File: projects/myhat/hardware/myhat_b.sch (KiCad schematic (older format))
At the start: 4 parts

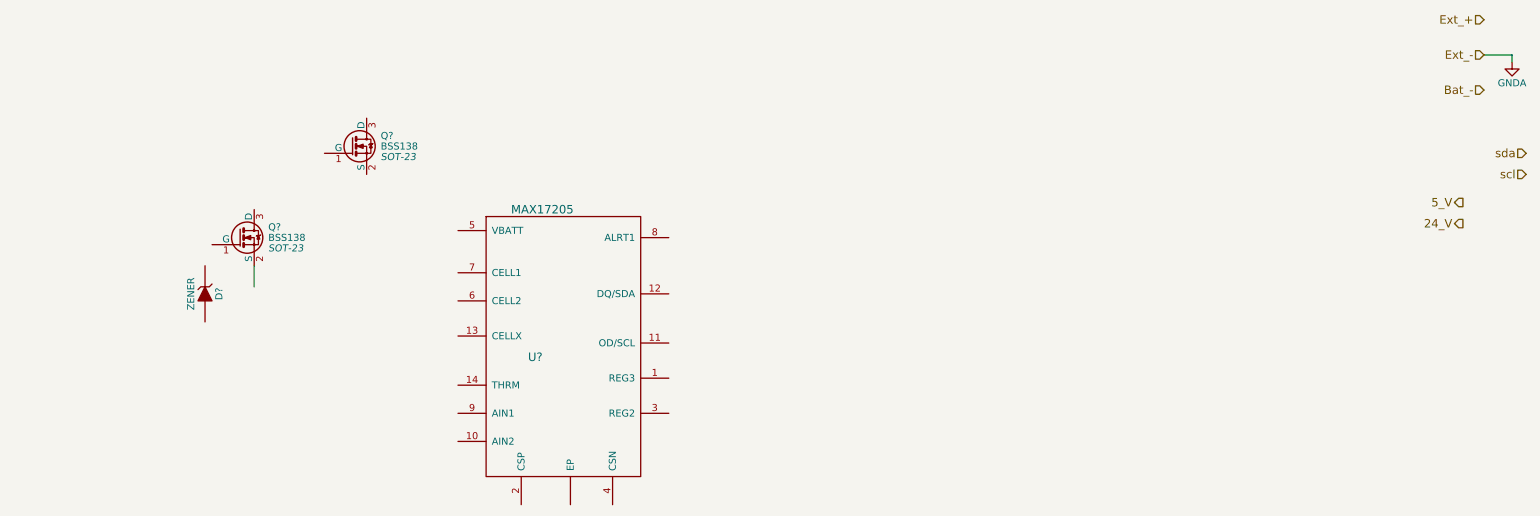
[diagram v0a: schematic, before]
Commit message: entered components on myhat for max17205
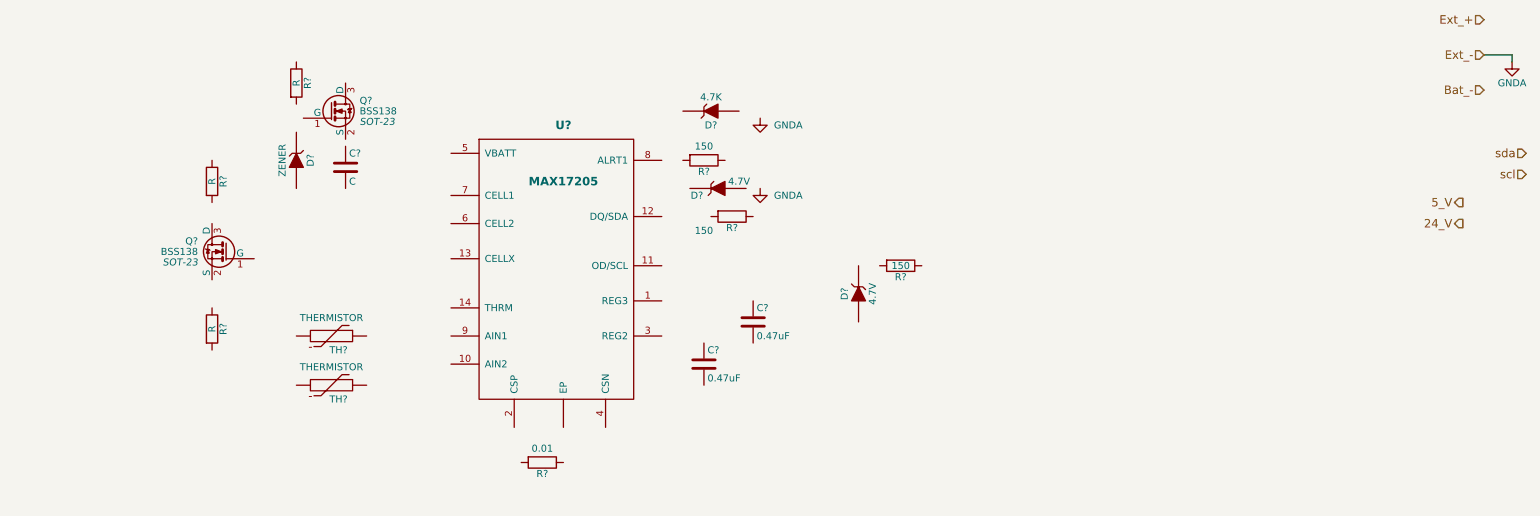
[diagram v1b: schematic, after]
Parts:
- removed U?: MAX17205, symbol MAX17205
- added C?: C, symbol C
- added C? (x2): 0.47uF, symbol C
- added D?: 4.7K, symbol ZENER
- added D? (x2): 4.7V, symbol ZENER
- added R? (x3): R, symbol R
- added R?: 0.01, symbol R
- added R? (x3): 150, symbol R
- added TH? (x2): THERMISTOR, symbol THERMISTOR
- added U?: MAX17205, symbol MAX17205
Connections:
- wire segments 3 -> 2
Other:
- moved on the sheet: D?, Q?
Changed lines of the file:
@@
 5_V
-$Comp
-L MAX17205 U?
-U 1 1 5838EF12
-P 3750 3550
-F 0 "U?" H 3400 3800 60  0000 C CNN
-F 1 "MAX17205" H 3450 4850 60  0000 C CNN
-F 2 "" H 3750 3550 60  0000 C CNN
-F 3 "" H 3750 3550 60  0000 C CNN
-	1    3750 3550
-	1    0    0    -1
-$EndComp
 $Comp
 L BSS138 Q?
 U 1 1 5838F608
-P 1300 2450
-F 0 "Q?" H 1500 2525 50  0000 L CNN
-F 1 "BSS138" H 1500 2450 50  0000 L CNN
-F 2 "SOT-23" H 1500 2375 50  0000 L CIN
-F 3 "" H 1300 2450 50  0000 L CNN
-	1    1300 2450
+P 1950 1550
+F 0 "Q?" H 2150 1625 50  0000 L CNN
+F 1 "BSS138" H 2150 1550 50  0000 L CNN
+F 2 "SOT-23" H 2150 1475 50  0000 L CIN
+F 3 "" H 1950 1550 50  0000 L CNN
+	1    1950 1550
 	1    0    0    -1
 $EndComp
@@
 L BSS138 Q?
 U 1 1 5838F9E4
-P 2100 1800
-F 0 "Q?" H 2300 1875 50  0000 L CNN
-F 1 "BSS138" H 2300 1800 50  0000 L CNN
-F 2 "SOT-23" H 2300 1725 50  0000 L CIN
-F 3 "" H 2100 1800 50  0000 L CNN
-	1    2100 1800
-	1    0    0    -1
-$EndComp
-Wire Wire Line
-	1400 2800 1400 2650
+P 1200 2550
+F 0 "Q?" H 1400 2625 50  0000 L CNN
+F 1 "BSS138" H 1400 2550 50  0000 L CNN
+F 2 "SOT-23" H 1400 2475 50  0000 L CIN
+F 3 "" H 1200 2550 50  0000 L CNN
+	1    1200 2550
+	-1   0    0    -1
+$EndComp
 $Comp
 L ZENER D?
 U 1 1 5839AB61
-P 1050 2850
-F 0 "D?" H 1050 2950 50  0000 C CNN
-F 1 "ZENER" H 1050 2750 50  0000 C CNN
-F 2 "" H 1050 2850 50  0000 C CNN
-F 3 "" H 1050 2850 50  0000 C CNN
-	1    1050 2850
+P 1700 1900
+F 0 "D?" H 1700 2000 50  0000 C CNN
+F 1 "ZENER" H 1700 1800 50  0000 C CNN
+F 2 "" H 1700 1900 50  0000 C CNN
+F 3 "" H 1700 1900 50  0000 C CNN
+	1    1700 1900
 	0    1    1    0
 $EndComp
@@
 Wire Wire Line
 	10350 1150 10350 1200
+$Comp
+L C C?
+U 1 1 583A4045
+P 2050 1950
+F 0 "C?" H 2075 2050 50  0000 L CNN
+F 1 "C" H 2075 1850 50  0000 L CNN
+F 2 "" H 2088 1800 50  0000 C CNN
+F 3 "" H 2050 1950 50  0000 C CNN
+	1    2050 1950
+	1    0    0    -1
+$EndComp
+$Comp
+L R R?
+U 1 1 583A42D9
+P 1100 2050
+F 0 "R?" V 1180 2050 50  0000 C CNN
+F 1 "R" V 1100 2050 50  0000 C CNN
+F 2 "" V 1030 2050 50  0000 C CNN
+F 3 "" H 1100 2050 50  0000 C CNN
+	1    1100 2050
+	1    0    0    -1
+$EndComp
+$Comp
+L R R?
+U 1 1 583A4306
+P 1700 1350
+F 0 "R?" V 1780 1350 50  0000 C CNN
+F 1 "R" V 1700 1350 50  0000 C CNN
+F 2 "" V 1630 1350 50  0000 C CNN
+F 3 "" H 1700 1350 50  0000 C CNN
+	1    1700 1350
+	1    0    0    -1
+$EndComp
+$Comp
+L R R?
+U 1 1 583A4395
+P 1100 3100
+F 0 "R?" V 1180 3100 50  0000 C CNN
+F 1 "R" V 1100 3100 50  0000 C CNN
+F 2 "" V 1030 3100 50  0000 C CNN
+F 3 "" H 1100 3100 50  0000 C CNN
+	1    1100 3100
+	1    0    0    -1
+$EndComp
+$Comp
+L MAX17205 U?
+U 1 1 583A5FF5
+P 3700 3000
+F 0 "U?" H 3600 4350 60  0000 C CNB
+F 1 "MAX17205" H 3600 3950 60  0000 C CNB
+F 2 "" H 3700 3000 60  0000 C CNN
+F 3 "" H 3700 3000 60  0000 C CNN
+	1    3700 3000
+	1    0    0    -1
+$EndComp
+$Comp
+L ZENER D?
+U 1 1 583A6504
+P 4650 1550
+F 0 "D?" H 4650 1650 50  0000 C CNN
+F 1 "4.7K" H 4650 1450 50  0000 C CNN
+F 2 "" H 4650 1550 50  0000 C CNN
+F 3 "" H 4650 1550 50  0000 C CNN
+	1    4650 1550
+	1    0    0    1
+$EndComp
+$Comp
+L ZENER D?
+U 1 1 583A661D
+P 4700 2100
+F 0 "D?" H 4550 2150 50  0000 C CNN
+F 1 "4.7V" H 4850 2050 50  0000 C CNN
+F 2 "" H 4700 2100 50  0000 C CNN
+F 3 "" H 4700 2100 50  0000 C CNN
+	1    4700 2100
+	1    0    0    1
+$EndComp
+$Comp
+L ZENER D?
+U 1 1 583A6665
+P 5700 2850
+F 0 "D?" H 5700 2950 50  0000 C CNN
+F 1 "4.7V" H 5700 2750 50  0000 C CNN
+F 2 "" H 5700 2850 50  0000 C CNN
+F 3 "" H 5700 2850 50  0000 C CNN
+	1    5700 2850
+	0    -1   1    0
+$EndComp
+$Comp
+L GNDA #PWR?
+U 1 1 583A66EB
+P 5000 1600
+F 0 "#PWR?" H 5000 1350 50  0001 C CNN
+F 1 "GNDA" H 5200 1550 50  0000 C CNN
+F 2 "" H 5000 1600 50  0000 C CNN
+F 3 "" H 5000 1600 50  0000 C CNN
+	1    5000 1600
+	1    0    0    -1
+$EndComp
+$Comp
+L GNDA #PWR?
+U 1 1 583A673F
+P 5000 2100
+F 0 "#PWR?" H 5000 1850 50  0001 C CNN
+F 1 "GNDA" H 5200 2050 50  0000 C CNN
+F 2 "" H 5000 2100 50  0000 C CNN
+F 3 "" H 5000 2100 50  0000 C CNN
+	1    5000 2100
+	1    0    0    -1
+$EndComp
+$Comp
+L C C?
+U 1 1 583A6F0A
+P 4950 3050
+F 0 "C?" H 4975 3150 50  0000 L CNN
+F 1 "0.47uF" H 4975 2950 50  0000 L CNN
+F 2 "" H 4988 2900 50  0000 C CNN
+F 3 "" H 4950 3050 50  0000 C CNN
+	1    4950 3050
+	1    0    0    -1
+$EndComp
+$Comp
+L C C?
+U 1 1 583A6FCE
+P 4600 3350
+F 0 "C?" H 4625 3450 50  0000 L CNN
+F 1 "0.47uF" H 4625 3250 50  0000 L CNN
+F 2 "" H 4638 3200 50  0000 C CNN
+F 3 "" H 4600 3350 50  0000 C CNN
+	1    4600 3350
+	1    0    0    -1
+$EndComp
+$Comp
+L R R?
+U 1 1 583A7028
+P 3450 4050
+F 0 "R?" V 3530 4050 50  0000 C CNN
+F 1 "0.01" V 3350 4050 50  0000 C CNN
+F 2 "" V 3380 4050 50  0000 C CNN
+F 3 "" H 3450 4050 50  0000 C CNN
+	1    3450 4050
+	0    1    1    0
+$EndComp
+$Comp
+L R R?
+U 1 1 583A7150
+P 4600 1900
+F 0 "R?" V 4680 1900 50  0000 C CNN
+F 1 "150" V 4500 1900 50  0000 C CNN
+F 2 "" V 4530 1900 50  0000 C CNN
+F 3 "" H 4600 1900 50  0000 C CNN
+	1    4600 1900
+	0    1    1    0
+$EndComp
+$Comp
+L R R?
+U 1 1 583A7259
+P 4800 2300
+F 0 "R?" V 4880 2300 50  0000 C CNN
+F 1 "150" V 4900 2100 50  0000 C CNN
+F 2 "" V 4730 2300 50  0000 C CNN
+F 3 "" H 4800 2300 50  0000 C CNN
+	1    4800 2300
+	0    1    1    0
+$EndComp
+$Comp
+L R R?
+U 1 1 583A72BD
+P 6000 2650
+F 0 "R?" V 6080 2650 50  0000 C CNN
+F 1 "150" V 6000 2650 50  0000 C CNN
+F 2 "" V 5930 2650 50  0000 C CNN
+F 3 "" H 6000 2650 50  0000 C CNN
+	1    6000 2650
+	0    1    1    0
+$EndComp
+$Comp
+L THERMISTOR TH?
+U 1 1 583B3F9B
+P 1950 3500
+F 0 "TH?" V 2050 3550 50  0000 C CNN
+F 1 "THERMISTOR" V 1850 3500 50  0000 C BNN
+F 2 "" H 1950 3500 50  0000 C CNN
+F 3 "" H 1950 3500 50  0000 C CNN
+	1    1950 3500
+	0    1    1    0
+$EndComp
+$Comp
+L THERMISTOR TH?
+U 1 1 583B3FD6
+P 1950 3150
+F 0 "TH?" V 2050 3200 50  0000 C CNN
+F 1 "THERMISTOR" V 1850 3150 50  0000 C BNN
+F 2 "" H 1950 3150 50  0000 C CNN
+F 3 "" H 1950 3150 50  0000 C CNN
+	1    1950 3150
+	0    1    1    0
+$EndComp
 $EndSCHEMATC

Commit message: updated footprints
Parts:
- R?: footprint (none) -> Resistors_SMD:R_0805_HandSoldering
- R? (x3): footprint (none) -> Resistors_SMD:R_0603_HandSoldering
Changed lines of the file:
@@
 F 0 "R?" V 3530 4050 50  0000 C CNN
 F 1 "0.01" V 3350 4050 50  0000 C CNN
-F 2 "" V 3380 4050 50  0000 C CNN
+F 2 "Resistors_SMD:R_0805_HandSoldering" V 3650 4050 50  0001 C CNN
 F 3 "" H 3450 4050 50  0000 C CNN
 	1    3450 4050
@@
 F 0 "R?" V 4680 1900 50  0000 C CNN
 F 1 "150" V 4500 1900 50  0000 C CNN
-F 2 "" V 4530 1900 50  0000 C CNN
+F 2 "Resistors_SMD:R_0603_HandSoldering" V 4530 1900 50  0001 C CNN
 F 3 "" H 4600 1900 50  0000 C CNN
 	1    4600 1900
@@
 P 4800 2300
 F 0 "R?" V 4880 2300 50  0000 C CNN
-F 1 "150" V 4900 2100 50  0000 C CNN
-F 2 "" V 4730 2300 50  0000 C CNN
+F 1 "150" V 4950 2300 50  0000 C CNN
+F 2 "Resistors_SMD:R_0603_HandSoldering" V 4730 2300 50  0001 C CNN
 F 3 "" H 4800 2300 50  0000 C CNN
 	1    4800 2300
@@
 P 6000 2650
 F 0 "R?" V 6080 2650 50  0000 C CNN
-F 1 "150" V 6000 2650 50  0000 C CNN
-F 2 "" V 5930 2650 50  0000 C CNN
+F 1 "150" V 6150 2650 50  0000 C CNN
+F 2 "Resistors_SMD:R_0603_HandSoldering" V 5930 2650 50  0001 C CNN
 F 3 "" H 6000 2650 50  0000 C CNN
 	1    6000 2650

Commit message: set component values for fuel gauge
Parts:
- added R?: 2.0M, Resistors_SMD:R_0805_HandSoldering, symbol R
- D?: value ZENER -> 18V; footprint (none) -> Diodes_SMD:SOD-323
- D?: value 4.7K -> 5.6V; footprint (none) -> Diodes_SMD:SOD-323
- D? (x2): value 4.7V -> 5.6V; footprint (none) -> Diodes_SMD:SOD-323
- R?: value R -> 300K; footprint (none) -> Resistors_SMD:R_0603_HandSoldering
- R?: value R -> 200k; footprint (none) -> Resistors_SMD:R_0603_HandSoldering
- TH? (x2): footprint (none) -> Resistors_SMD:R_0402
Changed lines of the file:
@@
 P 1700 1900
 F 0 "D?" H 1700 2000 50  0000 C CNN
-F 1 "ZENER" H 1700 1800 50  0000 C CNN
-F 2 "" H 1700 1900 50  0000 C CNN
+F 1 "18V" H 1700 1800 50  0000 C CNN
+F 2 "Diodes_SMD:SOD-323" H 1700 1900 50  0001 C CNN
 F 3 "" H 1700 1900 50  0000 C CNN
 	1    1700 1900
@@
 P 1100 2050
 F 0 "R?" V 1180 2050 50  0000 C CNN
-F 1 "R" V 1100 2050 50  0000 C CNN
-F 2 "" V 1030 2050 50  0000 C CNN
+F 1 "300K" V 1000 2050 50  0000 C CNN
+F 2 "Resistors_SMD:R_0603_HandSoldering" V 1030 2050 50  0001 C CNN
 F 3 "" H 1100 2050 50  0000 C CNN
 	1    1100 2050
@@
 P 1100 3100
 F 0 "R?" V 1180 3100 50  0000 C CNN
-F 1 "R" V 1100 3100 50  0000 C CNN
-F 2 "" V 1030 3100 50  0000 C CNN
+F 1 "200k" V 1100 3100 50  0000 C CNN
+F 2 "Resistors_SMD:R_0603_HandSoldering" V 1030 3100 50  0001 C CNN
 F 3 "" H 1100 3100 50  0000 C CNN
 	1    1100 3100
@@
 P 4650 1550
 F 0 "D?" H 4650 1650 50  0000 C CNN
-F 1 "4.7K" H 4650 1450 50  0000 C CNN
-F 2 "" H 4650 1550 50  0000 C CNN
+F 1 "5.6V" H 4650 1450 50  0000 C CNN
+F 2 "Diodes_SMD:SOD-323" H 4650 1550 50  0001 C CNN
 F 3 "" H 4650 1550 50  0000 C CNN
 	1    4650 1550
@@
 P 4700 2100
 F 0 "D?" H 4550 2150 50  0000 C CNN
-F 1 "4.7V" H 4850 2050 50  0000 C CNN
-F 2 "" H 4700 2100 50  0000 C CNN
+F 1 "5.6V" H 4850 2050 50  0000 C CNN
+F 2 "Diodes_SMD:SOD-323" H 4700 2100 50  0001 C CNN
 F 3 "" H 4700 2100 50  0000 C CNN
 	1    4700 2100
@@
 P 5700 2850
 F 0 "D?" H 5700 2950 50  0000 C CNN
-F 1 "4.7V" H 5700 2750 50  0000 C CNN
-F 2 "" H 5700 2850 50  0000 C CNN
+F 1 "5.6V" H 5700 2750 50  0000 C CNN
+F 2 "Diodes_SMD:SOD-323" H 5700 2850 50  0001 C CNN
 F 3 "" H 5700 2850 50  0000 C CNN
 	1    5700 2850
@@
 F 0 "TH?" V 2050 3550 50  0000 C CNN
 F 1 "THERMISTOR" V 1850 3500 50  0000 C BNN
-F 2 "" H 1950 3500 50  0000 C CNN
+F 2 "Resistors_SMD:R_0402" H 1950 3500 50  0001 C CNN
 F 3 "" H 1950 3500 50  0000 C CNN
 	1    1950 3500
@@
 F 0 "TH?" V 2050 3200 50  0000 C CNN
 F 1 "THERMISTOR" V 1850 3150 50  0000 C BNN
-F 2 "" H 1950 3150 50  0000 C CNN
+F 2 "Resistors_SMD:R_0402" H 1950 3150 50  0001 C CNN
 F 3 "" H 1950 3150 50  0000 C CNN
 	1    1950 3150
 	0    1    1    0
 $EndComp
+$Comp
+L R R?
+U 1 1 5840F9B7
+P 1100 1650
+F 0 "R?" V 1180 1650 50  0000 C CNN
+F 1 "2.0M" V 1000 1650 50  0000 C CNN
+F 2 "Resistors_SMD:R_0805_HandSoldering" V 1030 1650 50  0001 C CNN
+F 3 "" H 1100 1650 50  0000 C CNN
+	1    1100 1650
+	1    0    0    -1
+$EndComp
 $EndSCHEMATC

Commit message: updated hat_options
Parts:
- added R?: 1M, Resistors_SMD:R_0603_HandSoldering, symbol R
- added R? (x2): 10K, Resistors_SMD:R_0603_HandSoldering, symbol R
- C?: value C -> 1uF
- R?: value R -> 510K
- R?: value 150 -> 1K
- TH? (x2): value THERMISTOR -> 10K NTC
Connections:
- net Bat_-: now also R?.1, U?.4 (CSN), U?.~ (EP)
- net Ext_+: now also Q?.3 (D), R?.1, R?.1
- net GNDA: now also C?.2, C?.2, C?.2, D?.2 (A), D?.2 (A), D?.2 (A), D?.2 (A), R?.2, R?.2, TH?.1, TH?.1, U?.2 (CSP), U?.7 (CELL1), R?.1
- net scl: now also R?.1
- net sda: now also R?.1
- net at Q?.1 (G): now also D?.1 (K), R?.2
- net at Q?.2 (S): now also C?.1, U?.5 (VBATT)
- net at Q?.1 (G): now also U?.6 (CELL2), R?.2
- net at Q?.2 (S): now also R?.1, U?.13 (CELLX)
- net at Q?.3 (D): now also R?.2
- net at R?.1: now also R?.2
- net at U?.1 (REG3): now also C?.1
- net at U?.10 (AIN2): now also TH?.2, R?.1
- net at U?.11 (OD/SCL): now also D?.1 (K), R?.2
- net at U?.12 (DQ/SDA): now also D?.1 (K), R?.2
- net at U?.14 (THRM): now also R?.2, R?.2
- net at U?.3 (REG2): now also C?.1
- net at U?.8 (ALRT1): now also D?.1 (K), R?.2
- net at U?.9 (AIN1): now also TH?.2, R?.1
- net Bat_alert: now reaches R?.1
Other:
- moved on the sheet: D?, Q?, R?, TH?

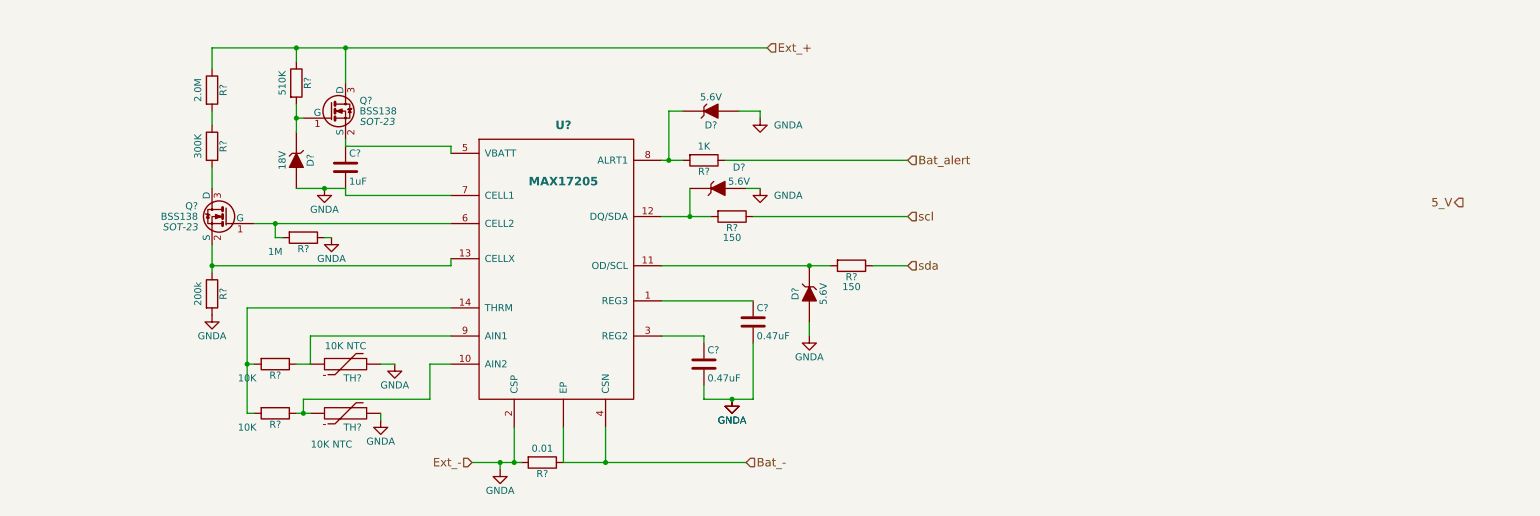
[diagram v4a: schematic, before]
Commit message: Added footprint for MAX17205
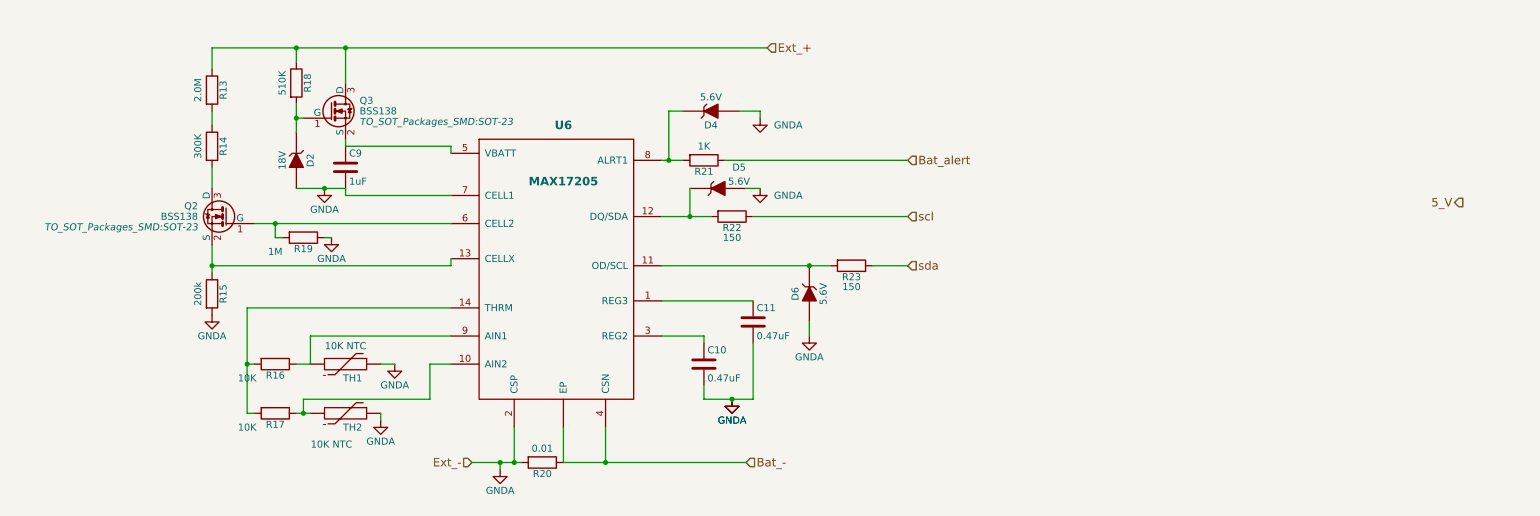
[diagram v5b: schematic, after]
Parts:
- C10, C11, C9: renamed from C?; footprint (none) -> Capacitors_SMD:C_0603_HandSoldering
- Q2, Q3: renamed from Q?; footprint SOT-23 -> TO_SOT_Packages_SMD:SOT-23
- R18: renamed from R?; footprint (none) -> Resistors_SMD:R_0603_HandSoldering
- U6: renamed from U?; footprint (none) -> Housings_DFN_QFN:DFN-14-1EP_3x4mm_Pitch0.5mm
- gave numbers to parts that had none: 16
